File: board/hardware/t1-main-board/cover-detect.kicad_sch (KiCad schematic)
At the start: 4 parts

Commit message: NFC reader withdrawn from the board, every model (BRD-057)
Maintainer decision 2026-10-27, reason: board area. blk.nfc-reader (#42)
withdrawn: PN7160, front end, crystal, antenna contacts, NFC_VBAT switch
and link #18 removed (35 parts). BRD-057 reworded: NFC as the dynamic tag
only; blk.nfc-tag stays. Pinout v1: 1N20, A37, B38 become unconnected
spares, expander P05 a spare. BOM v1.18 item 7 (line 50: 5 switches,
lines 127-128 withdrawn), power tree v0.10, variant files, feature blocks.

Sheets after the removed one move up a page; references renumbered in
plan.py, parts.py and the specs (J6201 -> J6101 and others).

Placement v1.4: 990 parts placed, board need 96.9 % (99.1 % before),
factor 1.72; 243 capacitors within bound; DRC 0 errors; ERC 0 errors;
craft Q1 met; overlaps 0; pcb tests pass; STEP exported.

Co-Authored-By: Claude Opus 5.5 <noreply@anthropic.com>
Claude-Session: https://claude.ai/code/session_01Ei262h3TpgY9vyfNLMi5Mn
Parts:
- removed D5901: TPD1E10B06, Package_SON:Texas_DPY0002A_0.6x1mm_P0.65mm, symbol Device:D_TVS
- removed R5901: 100 kΩ, Resistor_SMD:R_0201_0603Metric, symbol Device:R
- removed TP5901: COVER, TestPoint:TestPoint_Pad_2.0x2.0mm, symbol Connector:TestPoint
- removed TP5902: COVER_GND, TestPoint:TestPoint_Pad_2.0x2.0mm, symbol Connector:TestPoint
- added D5801: TPD1E10B06, Package_SON:Texas_DPY0002A_0.6x1mm_P0.65mm, symbol Device:D_TVS
- added R5801: 100 kΩ, Resistor_SMD:R_0201_0603Metric, symbol Device:R
- added TP5801: COVER, TestPoint:TestPoint_Pad_2.0x2.0mm, symbol Connector:TestPoint
- added TP5802: COVER_GND, TestPoint:TestPoint_Pad_2.0x2.0mm, symbol Connector:TestPoint
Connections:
- net COVER_DET_N: now also D5801.2 (A2), R5801.2, TP5801.1
- net GND: now also D5801.1 (A1), TP5802.1
- net vcc3v3_pmu: now also R5801.1
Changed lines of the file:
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@@
 (title_block (title "Cover detect") (date "2026-10-25") (rev "A") (company "The OpenDAP Project") (comment 1 "blk.cover-detect") (comment 2 "Back-cover detect input: board-edge contact pads, pull-up, ESD"))
 (symbol (lib_id "Connector:TestPoint") (at 39.37 45.72 0) (unit 1) (body_style 1) (exclude_from_sim no) (in_bom no) (on_board yes) (dnp no)
-  (property "Reference" "TP5901" (at 38.1 40.64 0) (effects (font (size 1.27 1.27)) (justify right)))
+  (property "Reference" "TP5801" (at 38.1 40.64 0) (effects (font (size 1.27 1.27)) (justify right)))
   (property "Value" "COVER" (at 38.1 43.18 0) (effects (font (size 1.27 1.27)) (justify right)))
   (property "Footprint" "TestPoint:TestPoint_Pad_2.0x2.0mm" (at 39.37 45.72 0) (effects (font (size 1.27 1.27))) (hide yes))
@@
   (property "Block" "blk.cover-detect" (at 39.37 45.72 0) (effects (font (size 1.27 1.27))) (hide yes))
   (pin "1")
-  (instances (project "t1-main-board" (path "/7746052e-d7f9-59ad-ba73-bd2b74439529/357cd0ed-ef3a-5696-a4d8-7fa96210e511" (reference "TP5901") (unit 1))))
+  (instances (project "t1-main-board" (path "/7746052e-d7f9-59ad-ba73-bd2b74439529/357cd0ed-ef3a-5696-a4d8-7fa96210e511" (reference "TP5801") (unit 1))))
 )
 (symbol (lib_id "Connector:TestPoint") (at 64.77 45.72 0) (unit 1) (body_style 1) (exclude_from_sim no) (in_bom no) (on_board yes) (dnp no)
-  (property "Reference" "TP5902" (at 63.5 40.64 0) (effects (font (size 1.27 1.27)) (justify right)))
+  (property "Reference" "TP5802" (at 63.5 40.64 0) (effects (font (size 1.27 1.27)) (justify right)))
   (property "Value" "COVER_GND" (at 63.5 43.18 0) (effects (font (size 1.27 1.27)) (justify right)))
   (property "Footprint" "TestPoint:TestPoint_Pad_2.0x2.0mm" (at 64.77 45.72 0) (effects (font (size 1.27 1.27))) (hide yes))
@@
   (property "Block" "blk.cover-detect" (at 64.77 45.72 0) (effects (font (size 1.27 1.27))) (hide yes))
   (pin "1")
-  (instances (project "t1-main-board" (path "/7746052e-d7f9-59ad-ba73-bd2b74439529/357cd0ed-ef3a-5696-a4d8-7fa96210e511" (reference "TP5902") (unit 1))))
+  (instances (project "t1-main-board" (path "/7746052e-d7f9-59ad-ba73-bd2b74439529/357cd0ed-ef3a-5696-a4d8-7fa96210e511" (reference "TP5802") (unit 1))))
 )
 (wire (pts (xy 64.77 45.72) (xy 64.77 48.26)) (stroke (width 0) (type default)))
 (symbol (lib_id "power:GND") (at 64.77 48.26 0) (unit 1) (body_style 1) (exclude_from_sim no) (in_bom yes) (on_board yes) (dnp no)
-  (property "Reference" "#PWR0944" (at 64.77 48.26 0) (effects (font (size 1.27 1.27))) (hide yes))
+  (property "Reference" "#PWR0915" (at 64.77 48.26 0) (effects (font (size 1.27 1.27))) (hide yes))
   (property "Value" "GND" (at 64.77 52.07 0) (effects (font (size 1.27 1.27))))
   (property "Footprint" "" (at 64.77 48.26 0) (effects (font (size 1.27 1.27))) (hide yes))
   (property "Datasheet" "" (at 64.77 48.26 0) (effects (font (size 1.27 1.27))) (hide yes))
   (pin "1")
-  (instances (project "t1-main-board" (path "/7746052e-d7f9-59ad-ba73-bd2b74439529/357cd0ed-ef3a-5696-a4d8-7fa96210e511" (reference "#PWR0944") (unit 1))))
+  (instances (project "t1-main-board" (path "/7746052e-d7f9-59ad-ba73-bd2b74439529/357cd0ed-ef3a-5696-a4d8-7fa96210e511" (reference "#PWR0915") (unit 1))))
 )
 (rectangle (start 22.86 35.56) (end 158.75 63.5) (stroke (width 0) (type dash)) (fill (type none)))
 (text "Contact pads at the board edge (BOM v1 line 143; PCB-L-10)" (exclude_from_sim no) (at 24.13 34.29 0) (effects (font (size 2.54 2.54)) (justify left bottom)))
 (symbol (lib_id "Device:R") (at 175.26 48.26 0) (unit 1) (body_style 1) (exclude_from_sim no) (in_bom yes) (on_board yes) (dnp no)
-  (property "Reference" "R5901" (at 176.53 46.99 0) (effects (font (size 1.27 1.27)) (justify left)))
+  (property "Reference" "R5801" (at 176.53 46.99 0) (effects (font (size 1.27 1.27)) (justify left)))
   (property "Value" "100 kΩ" (at 176.53 49.53 0) (effects (font (size 1.27 1.27)) (justify left)))
   (property "Footprint" "Resistor_SMD:R_0201_0603Metric" (at 175.26 48.26 0) (effects (font (size 1.27 1.27))) (hide yes))
@@
   (pin "1")
   (pin "2")
-  (instances (project "t1-main-board" (path "/7746052e-d7f9-59ad-ba73-bd2b74439529/357cd0ed-ef3a-5696-a4d8-7fa96210e511" (reference "R5901") (unit 1))))
+  (instances (project "t1-main-board" (path "/7746052e-d7f9-59ad-ba73-bd2b74439529/357cd0ed-ef3a-5696-a4d8-7fa96210e511" (reference "R5801") (unit 1))))
 )
 (wire (pts (xy 175.26 44.45) (xy 175.26 41.91)) (stroke (width 0) (type default)))
 (symbol (lib_id "power:VCC") (at 175.26 41.91 0) (unit 1) (body_style 1) (exclude_from_sim no) (in_bom yes) (on_board yes) (dnp no)
-  (property "Reference" "#PWR0945" (at 175.26 41.91 0) (effects (font (size 1.27 1.27))) (hide yes))
+  (property "Reference" "#PWR0916" (at 175.26 41.91 0) (effects (font (size 1.27 1.27))) (hide yes))
   (property "Value" "vcc3v3_pmu" (at 175.26 38.1 0) (effects (font (size 1.27 1.27))))
   (property "Footprint" "" (at 175.26 41.91 0) (effects (font (size 1.27 1.27))) (hide yes))
   (property "Datasheet" "" (at 175.26 41.91 0) (effects (font (size 1.27 1.27))) (hide yes))
   (pin "1")
-  (instances (project "t1-main-board" (path "/7746052e-d7f9-59ad-ba73-bd2b74439529/357cd0ed-ef3a-5696-a4d8-7fa96210e511" (reference "#PWR0945") (unit 1))))
+  (instances (project "t1-main-board" (path "/7746052e-d7f9-59ad-ba73-bd2b74439529/357cd0ed-ef3a-5696-a4d8-7fa96210e511" (reference "#PWR0916") (unit 1))))
 )
 (rectangle (start 163.83 35.56) (end 214.63 71.12) (stroke (width 0) (type dash)) (fill (type none)))
 (text "Pull-up to vcc3v3_pmu" (exclude_from_sim no) (at 165.1 34.29 0) (effects (font (size 2.54 2.54)) (justify left bottom)))
 (symbol (lib_id "Device:D_TVS") (at 30.48 104.14 90) (unit 1) (body_style 1) (exclude_from_sim no) (in_bom yes) (on_board yes) (dnp no)
-  (property "Reference" "D5901" (at 35.92 102.87 90) (effects (font (size 1.27 1.27))))
+  (property "Reference" "D5801" (at 35.92 102.87 90) (effects (font (size 1.27 1.27))))
   (property "Value" "TPD1E10B06" (at 38.82 105.41 90) (effects (font (size 1.27 1.27))))
   (property "Footprint" "Package_SON:Texas_DPY0002A_0.6x1mm_P0.65mm" (at 30.48 104.14 0) (effects (font (size 1.27 1.27))) (hide yes))
@@
   (pin "1")
   (pin "2")
-  (instances (project "t1-main-board" (path "/7746052e-d7f9-59ad-ba73-bd2b74439529/357cd0ed-ef3a-5696-a4d8-7fa96210e511" (reference "D5901") (unit 1))))
+  (instances (project "t1-main-board" (path "/7746052e-d7f9-59ad-ba73-bd2b74439529/357cd0ed-ef3a-5696-a4d8-7fa96210e511" (reference "D5801") (unit 1))))
 )
 (wire (pts (xy 30.48 100.33) (xy 30.48 97.79)) (stroke (width 0) (type default)))
 (wire (pts (xy 30.48 107.95) (xy 30.48 110.49)) (stroke (width 0) (type default)))
 (symbol (lib_id "power:GND") (at 30.48 110.49 0) (unit 1) (body_style 1) (exclude_from_sim no) (in_bom yes) (on_board yes) (dnp no)
-  (property "Reference" "#PWR0946" (at 30.48 110.49 0) (effects (font (size 1.27 1.27))) (hide yes))
+  (property "Reference" "#PWR0917" (at 30.48 110.49 0) (effects (font (size 1.27 1.27))) (hide yes))
   (property "Value" "GND" (at 30.48 114.3 0) (effects (font (size 1.27 1.27))))
   (property "Footprint" "" (at 30.48 110.49 0) (effects (font (size 1.27 1.27))) (hide yes))
   (property "Datasheet" "" (at 30.48 110.49 0) (effects (font (size 1.27 1.27))) (hide yes))
   (pin "1")
-  (instances (project "t1-main-board" (path "/7746052e-d7f9-59ad-ba73-bd2b74439529/357cd0ed-ef3a-5696-a4d8-7fa96210e511" (reference "#PWR0946") (unit 1))))
+  (instances (project "t1-main-board" (path "/7746052e-d7f9-59ad-ba73-bd2b74439529/357cd0ed-ef3a-5696-a4d8-7fa96210e511" (reference "#PWR0917") (unit 1))))
 )
 (rectangle (start 22.86 81.28) (end 87.63 119.38) (stroke (width 0) (type dash)) (fill (type none)))

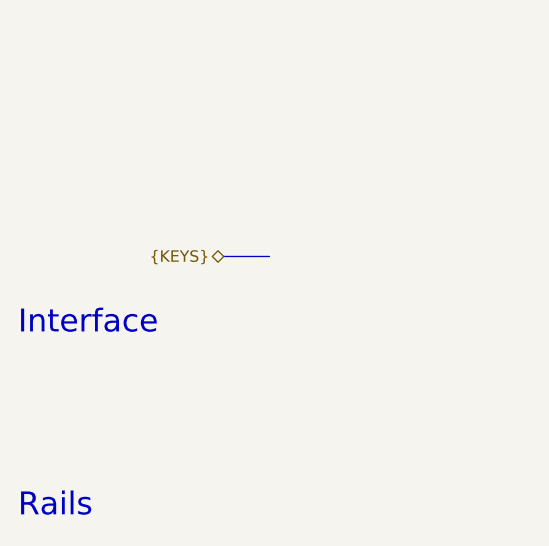
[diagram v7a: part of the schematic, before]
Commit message: Variants: devicetree nodes, host-side absent pulls, board variant data
Feature blocks: every record with a devicetree node names it; Sub-blocks
rows for the 16 sheet IDs. The RP2354 and HPA_RAIL_EN absent-state
pull-downs move to blk.soc-vccio-b, so they stay when the block is not
fitted; cover detect relies on the ball's own pull-down. pcb/variants.py
copies the schematic's production data onto the board. odapkit variant
check: full and production pass, reproducible.

The PTS815 land drawn from the C&K data sheet (p. B-44); the side buttons
respaced for it (PCB-Z-08 updated). Studies find repos.tsv by walking up
and use libs' rockchip.pretty. DRC 0 errors, ERC 0 errors, craft Q1 met,
pcb tests pass (33), 994 parts placed, 99.7 % board need, factor 1.64.

Co-Authored-By: Claude Opus 5.5 <noreply@anthropic.com>
Claude-Session: https://claude.ai/code/session_013P6pW9LdyEMFishwCcZGUr
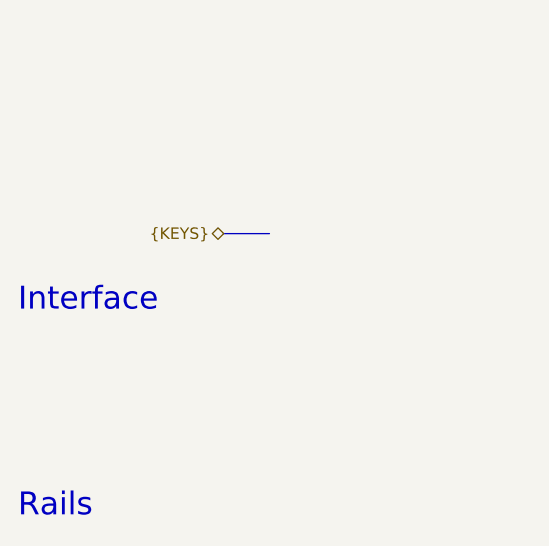
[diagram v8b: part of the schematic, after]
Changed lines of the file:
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@@
 (text "Rails" (exclude_from_sim no) (at 22.86 179.07 0) (effects (font (size 2.54 2.54)) (justify left bottom)))
 (table (column_count 3) (border (external yes) (header yes) (stroke (width 0) (type solid))) (separators (rows yes) (cols yes) (stroke (width 0) (type solid))) (column_widths 27.94 39.37 54.61) (row_heights 5.08 7.62) (cells (table_cell "Rail" (exclude_from_sim no) (at 22.86 180.34 0) (size 27.94 5.08) (margins 0.9525 0.9525 0.9525 0.9525) (span 1 1) (fill (type none)) (effects (font (size 1.27 1.27) (bold yes)) (justify left top))) (table_cell "Capacitors" (exclude_from_sim no) (at 50.8 180.34 0) (size 39.37 5.08) (margins 0.9525 0.9525 0.9525 0.9525) (span 1 1) (fill (type none)) (effects (font (size 1.27 1.27) (bold yes)) (justify left top))) (table_cell "Requirement and source" (exclude_from_sim no) (at 90.17 180.34 0) (size 54.61 5.08) (margins 0.9525 0.9525 0.9525 0.9525) (span 1 1) (fill (type none)) (effects (font (size 1.27 1.27) (bold yes)) (justify left top))) (table_cell "(none)" (exclude_from_sim no) (at 22.86 185.42 0) (size 27.94 7.62) (margins 0.9525 0.9525 0.9525 0.9525) (span 1 1) (fill (type none)) (effects (font (size 1.27 1.27)) (justify left top))) (table_cell "-" (exclude_from_sim no) (at 50.8 185.42 0) (size 39.37 7.62) (margins 0.9525 0.9525 0.9525 0.9525) (span 1 1) (fill (type none)) (effects (font (size 1.27 1.27)) (justify left top))) (table_cell "No supply on this sheet: the pull-up hangs from vcc3v3_pmu" (exclude_from_sim no) (at 90.17 185.42 0) (size 54.61 7.62) (margins 0.9525 0.9525 0.9525 0.9525) (span 1 1) (fill (type none)) (effects (font (size 1.27 1.27)) (justify left top)))))
-(text "Interface" (exclude_from_sim no) (at 22.86 158.75 0) (effects (font (size 2.54 2.54)) (justify left bottom)))
-(table (column_count 3) (border (external yes) (header yes) (stroke (width 0) (type solid))) (separators (rows yes) (cols yes) (stroke (width 0) (type solid))) (column_widths 45.72 25.4 50.8) (row_heights 5.08 7.62) (cells (table_cell "Net" (exclude_from_sim no) (at 22.86 160.02 0) (size 45.72 5.08) (margins 0.9525 0.9525 0.9525 0.9525) (span 1 1) (fill (type none)) (effects (font (size 1.27 1.27) (bold yes)) (justify left top))) (table_cell "Direction" (exclude_from_sim no) (at 68.58 160.02 0) (size 25.4 5.08) (margins 0.9525 0.9525 0.9525 0.9525) (span 1 1) (fill (type none)) (effects (font (size 1.27 1.27) (bold yes)) (justify left top))) (table_cell "Absent state (block not fitted)" (exclude_from_sim no) (at 93.98 160.02 0) (size 50.8 5.08) (margins 0.9525 0.9525 0.9525 0.9525) (span 1 1) (fill (type none)) (effects (font (size 1.27 1.27) (bold yes)) (justify left top))) (table_cell "COVER_DET_N" (exclude_from_sim no) (at 22.86 165.1 0) (size 45.72 7.62) (margins 0.9525 0.9525 0.9525 0.9525) (span 1 1) (fill (type none)) (effects (font (size 1.27 1.27)) (justify left top))) (table_cell "Output" (exclude_from_sim no) (at 68.58 165.1 0) (size 25.4 7.62) (margins 0.9525 0.9525 0.9525 0.9525) (span 1 1) (fill (type none)) (effects (font (size 1.27 1.27)) (justify left top))) (table_cell "GPIO0_A6 reset pull-down reads cover closed; the description omits the input (dnp)" (exclude_from_sim no) (at 93.98 165.1 0) (size 50.8 7.62) (margins 0.9525 0.9525 0.9525 0.9525) (span 1 1) (fill (type none)) (effects (font (size 1.27 1.27)) (justify left top)))))
+(text "Interface" (exclude_from_sim no) (at 22.86 156.21 0) (effects (font (size 2.54 2.54)) (justify left bottom)))
+(table (column_count 3) (border (external yes) (header yes) (stroke (width 0) (type solid))) (separators (rows yes) (cols yes) (stroke (width 0) (type solid))) (column_widths 45.72 25.4 50.8) (row_heights 5.08 10.16) (cells (table_cell "Net" (exclude_from_sim no) (at 22.86 157.48 0) (size 45.72 5.08) (margins 0.9525 0.9525 0.9525 0.9525) (span 1 1) (fill (type none)) (effects (font (size 1.27 1.27) (bold yes)) (justify left top))) (table_cell "Direction" (exclude_from_sim no) (at 68.58 157.48 0) (size 25.4 5.08) (margins 0.9525 0.9525 0.9525 0.9525) (span 1 1) (fill (type none)) (effects (font (size 1.27 1.27) (bold yes)) (justify left top))) (table_cell "Absent state (block not fitted)" (exclude_from_sim no) (at 93.98 157.48 0) (size 50.8 5.08) (margins 0.9525 0.9525 0.9525 0.9525) (span 1 1) (fill (type none)) (effects (font (size 1.27 1.27) (bold yes)) (justify left top))) (table_cell "COVER_DET_N" (exclude_from_sim no) (at 22.86 162.56 0) (size 45.72 10.16) (margins 0.9525 0.9525 0.9525 0.9525) (span 1 1) (fill (type none)) (effects (font (size 1.27 1.27)) (justify left top))) (table_cell "Output" (exclude_from_sim no) (at 68.58 162.56 0) (size 25.4 10.16) (margins 0.9525 0.9525 0.9525 0.9525) (span 1 1) (fill (type none)) (effects (font (size 1.27 1.27)) (justify left top))) (table_cell "The SoC ball's own reset pull-down (GPIO0_A6) reads cover closed; the description omits the input (dnp)" (exclude_from_sim no) (at 93.98 162.56 0) (size 50.8 10.16) (margins 0.9525 0.9525 0.9525 0.9525) (span 1 1) (fill (type none)) (effects (font (size 1.27 1.27)) (justify left top)))))
 (label "COVER_DET_N" (at 39.37 45.72 270) (effects (font (size 1.27 1.27)) (justify right bottom)))
 (label "COVER_DET_N" (at 175.26 52.07 270) (effects (font (size 1.27 1.27)) (justify right bottom)))
 (label "COVER_DET_N" (at 30.48 97.79 90) (effects (font (size 1.27 1.27)) (justify left bottom)))
-(bus (pts (xy 45.72 149.86) (xy 50.8 149.86)) (stroke (width 0) (type default)))
-(hierarchical_label "{KEYS}" (shape bidirectional) (at 45.72 149.86 180) (effects (font (size 1.27 1.27)) (justify right)))
+(bus (pts (xy 45.72 147.32) (xy 50.8 147.32)) (stroke (width 0) (type default)))
+(hierarchical_label "{KEYS}" (shape bidirectional) (at 45.72 147.32 180) (effects (font (size 1.27 1.27)) (justify right)))
 (embedded_fonts no))
